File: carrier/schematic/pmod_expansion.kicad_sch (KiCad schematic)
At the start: 14 parts, among them J19001 DS1024-2x6R2, SW19001 DSHP04TSGER, U19001 SY6280AAC, U19002 TPD4E1U06, U19003 TPD4E1U06

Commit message: bom: sourcing risk+cost report + C1591->C14663 (Extended->Basic 100n)
Stream F — live JLCPCB/LCSC sourcing pass over all 95 distinct BOM parts.

Report: carrier/manufacturing/SOURCING.md — per-part stock / Basic-vs-Extended
/ unit price / risk + flagged second sources, and a rollup (94 parts post-swap,
64 Extended of which 2 Preferred -> 62 feeder fees = ~$186, 15 parts <5k stock,
6 procurement-critical <300). Data from the JLCPCB parts API (live).

Applied swap (only clean Basic drop-in on the board): 100 nF 0603 decoupling
C1591 (Samsung CL10B104KB8NNNC, Extended, 2.08M) -> C14663 (YAGEO
CC0603KRX7R9BB104, Basic, 17.8M). IDENTICAL 100nF/50V/X7R/+-10%/0603, same
footprint+symbol -> netlist & render byte-identical; ratings.py already carries
C14663 with matching ratings. Merges 71 Extended + 12 existing-Basic positions
onto one 83-piece Basic line: removes one Extended feeder fee, cheaper unit,
8.5x more stock.

Everything else is REPORT-ONLY: every other Extended part is
Extended-by-necessity (no JLC-Basic equivalent — precise E96 values, specialty
ICs/connectors) or has only a footprint-mismatched / MPN-ambiguous alternate.
Also flagged (not fixed): C25750 ("40.2k" power:R1) currently resolves on LCSC
to a 120k 0402 part — a data-integrity bug; recommend C12447 after intent check.

Gates: part-rules PASS (132 checks, 0 findings); board PASS (33 sheets, golden
renders 33/33 match, DRC 0); selftest 59/59; m1_rc PASS; pytest 219 passed.
BOM regen deterministic (md5 stable).

Co-Authored-By: Claude Opus 4.8 <noreply@anthropic.com>
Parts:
- C19001, C19002, C19003: LCSC C1591 -> C14663
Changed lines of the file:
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@@
 		(property
 			"LCSC"
-			"C1591"
+			"C14663"
 			(at 29.21 66.04 0)
 			(effects
@@
 		(property
 			"LCSC"
-			"C1591"
+			"C14663"
 			(at 39.37 66.04 0)
 			(effects
@@
 		(property
 			"LCSC"
-			"C1591"
+			"C14663"
 			(at 49.53 66.04 0)
 			(effects

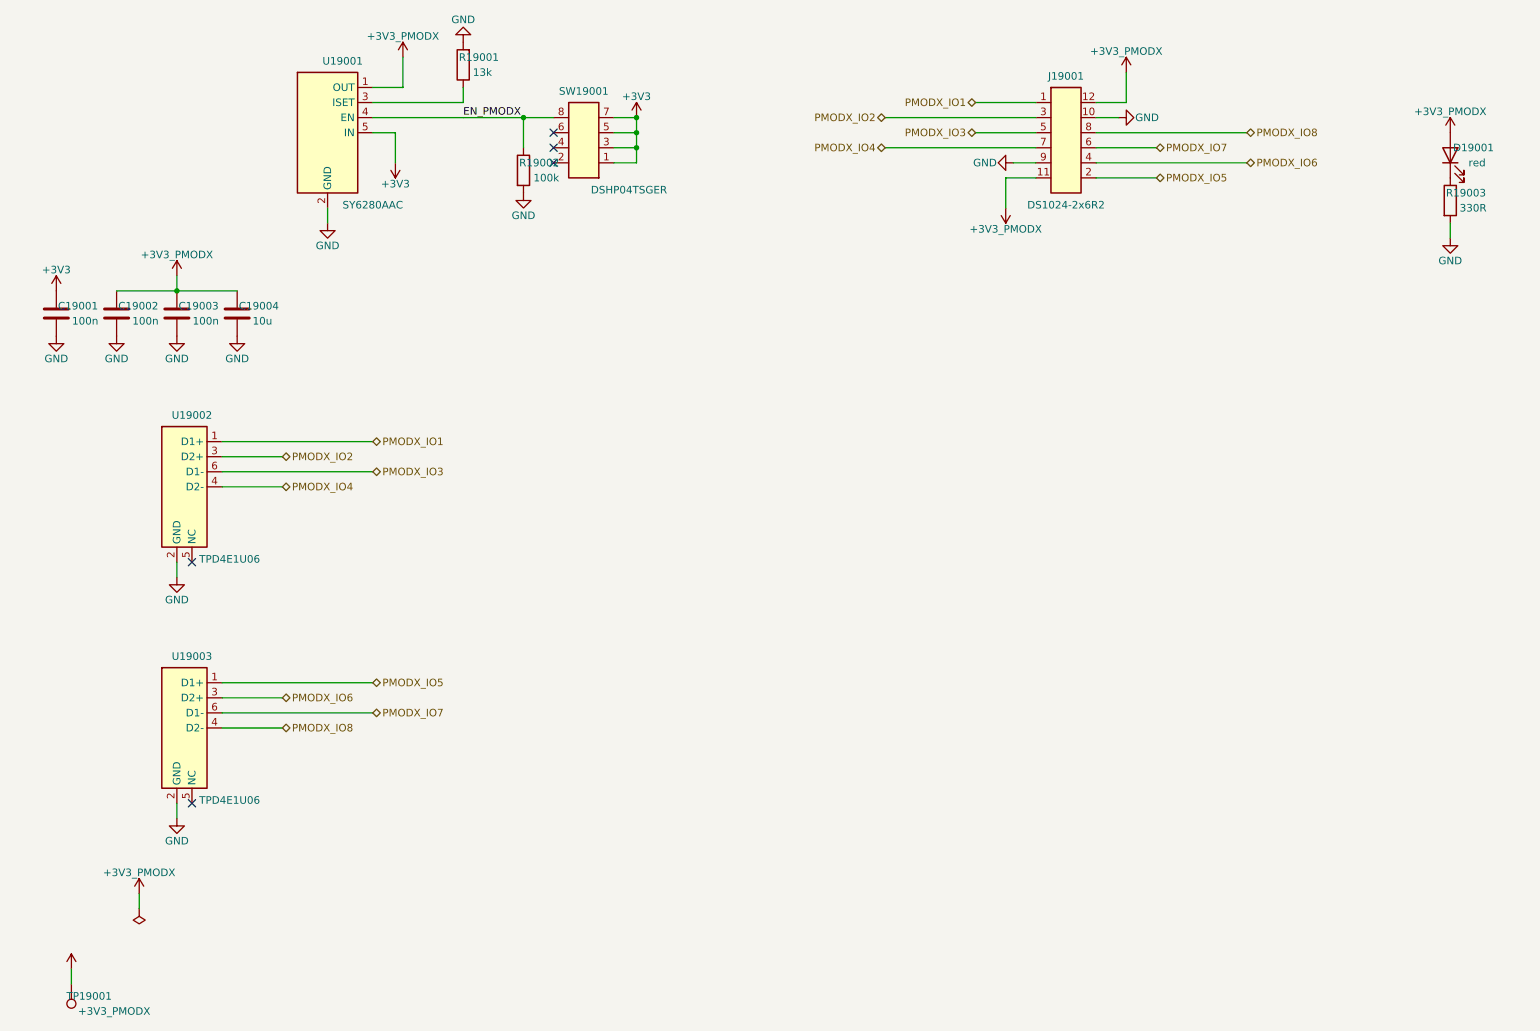
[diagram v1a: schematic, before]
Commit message: carrier: 4 confirmed datasheet-audit fixes (crystal CL, LED Vf, SY6280 Cin, LVC125 doc)
All four adversarially re-verified against the datasheet + schematic before
applying:

- usb_jtag-1 (crystal load caps): Y1 (KDS DSX321G, CL=12pF) had two 22pF load
  caps presenting ~15pF -> 8MHz pulled ~-50..-90ppm (outside ±20ppm). 22p->16p
  C0G 0603 (Cext = 2·(CL-~4pF stray)); LCSC C162205 (Murata GRM1885C1H160JA01D,
  16pF C0G 50V 0603, live-verified).
- usb_jtag-2 (SN74LVC125A): removed the false "Ioff partial-power-down" docstring
  claim (TI SCAS290T has no such spec); powered-rail Hi-Z holds via the normal
  3-state OE pull-up. Series back-feed Rs documented as a DNP/layout reservation
  (forcing them overflows the A3 sheet; not fitted).
- io_misc-1 (user LED current): +3V3_USER_LED through 1k gave ~0.2mA (invisible)
  for the high-Vf (~3.1V) green/blue/white LEDs. Per-colour Rs: red keeps 1k
  (~1.3mA); green/blue/white -> 200R (C8218), ~1-3.5mA, within the 5mA rating.
- expansion-1 (SY6280 Cin): the load-switch IN pin had only 100n; added the
  datasheet-mandated 10uF (C15850) bulk at U1.IN, kept the 100n.

BOM VALUES now 0 unverified (white LED C2290 catalogued). Regression: board 33
+ golden match, all gates PASS, selftest 59, m1_rc, pytest 242 — green.

Co-Authored-By: Claude Opus 4.8 <noreply@anthropic.com>
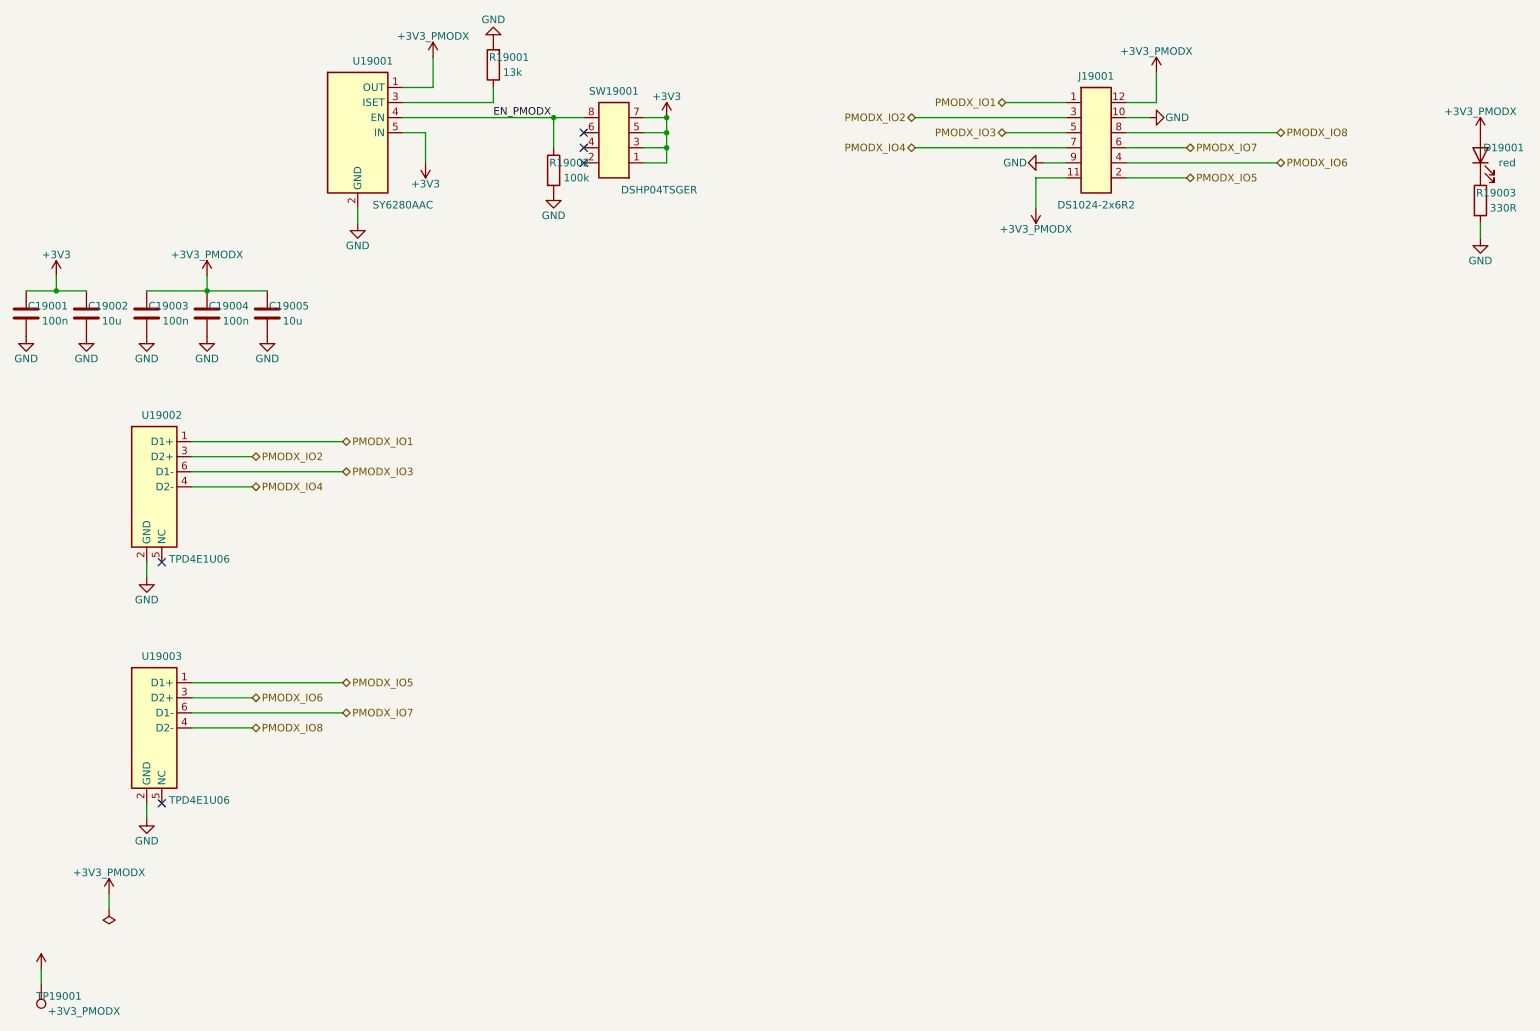
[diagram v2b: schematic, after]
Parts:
- added TP19001: +3V3_PMODX, TestPoint:TestPoint_Pad_D1.5mm, symbol Connector:TestPoint
- C19002: value 100n -> 10u; footprint Capacitor_SMD:C_0603_1608Metric -> Capacitor_SMD:C_0805_2012Metric; LCSC C14663 -> C15850
- C19004: value 10u -> 100n; footprint Capacitor_SMD:C_0805_2012Metric -> Capacitor_SMD:C_0603_1608Metric; LCSC C15850 -> C14663
- C19005: renamed from U19002; value TPD4E1U06 -> 10u; footprint TPD4E1U06DBVR:TPD4E1U06DBVR -> Capacitor_SMD:C_0805_2012Metric; symbol TPD4E1U06DBVR:TPD4E1U06DBVR -> Device:C; LCSC C124691 -> C15850
- D19001: renamed from R19003; value 330R -> red; footprint Resistor_SMD:R_0603_1608Metric -> LED_SMD:LED_0603_1608Metric; symbol Device:R -> Device:LED; LCSC C23138 -> C2286
- R19003: renamed from TP19001; value +3V3_PMODX -> 330R; footprint TestPoint:TestPoint_Pad_D1.5mm -> Resistor_SMD:R_0603_1608Metric; symbol Connector:TestPoint -> Device:R; BOM exclude -> (none); LCSC (none) -> C23138
- U19003: renamed from D19001; value red -> TPD4E1U06; footprint LED_SMD:LED_0603_1608Metric -> TPD4E1U06DBVR:TPD4E1U06DBVR; symbol Device:LED -> TPD4E1U06DBVR:TPD4E1U06DBVR; LCSC C2286 -> C124691
- renumbered U19003 to U19002
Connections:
- net +3V3: now also C19002.1
- net +3V3_PMODX: now also C19005.1, D19001.2 (A), TP19001.1; no longer C19002.1, R19003.1, U19003.2 (A)
- net GND: now also R19003.2, U19003.2 (GND); no longer D19001.2
- net PMODX_IO1: now also U19002.1 (D1+); no longer C19005.1 (D1+)
- net PMODX_IO2: now also U19002.3 (D2+); no longer C19005.3 (D2+)
- net PMODX_IO3: now also U19002.6 (D1-); no longer C19005.6 (D1-)
- net PMODX_IO4: now also U19002.4 (D2-); no longer C19005.4 (D2-)
- net PMODX_IO5: now also U19003.1 (D1+); no longer U19002.1 (D1+)
- net PMODX_IO6: now also U19003.3 (D2+); no longer U19002.3 (D2+)
- net PMODX_IO7: now also U19003.6 (D1-); no longer U19002.6 (D1-)
- net PMODX_IO8: now also U19003.4 (D2-); no longer U19002.4 (D2-)
- net at D19001.1 (K): now also R19003.1; no longer U19003.1 (K)
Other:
- moved on the sheet: C19001, C19002, C19003, C19004, J19001, R19001, R19002, SW19001, U19001, U19002

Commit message: fix(silk): tighten 6 sheet titles overflowing the title-block cell (M6)
The audit flagged 6 sheet titles whose text overflowed the KiCad title-block
Title cell, crossing the border/zone rules (LAW 1). Root cause: the authored
Circuit titles were longer than the cell renders (the fit boundary is ~58 chars
of typical text; these were 55-73). Tightened all 6 at the source (display-only
strings, no info-loss of the essentials, cannot affect netlist/routing — board
.kicad_pcb byte-unchanged):
- board_services 73->47, pmod_expansion 65->45, mechanical 60->50,
  usb_jtag 59->38, usb_jtag_connector 58->42, power_som 55->37.
Render-confirmed: board_services + mechanical (the longest) now end well inside
the cell. The gallery description table (carrier/README.md) regenerated to match.
666 tests pass at HEAD; the 3 title-asserting tests (som_j1/j2/j3) are untouched.

Co-Authored-By: Claude Opus 4.8 <noreply@anthropic.com>
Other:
- title: Pmod expansion port (2x6, bank 13, low-cap ESD, manual-gated 3V3) -> Pmod expansion (2x6, bank 13, ESD, gated 3V3)
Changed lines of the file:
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@@
 	(paper "A4")
 	(title_block
-		(title "Pmod expansion port (2x6, bank 13, low-cap ESD, manual-gated 3V3)")
+		(title "Pmod expansion (2x6, bank 13, ESD, gated 3V3)")
 		(company "Zynq SoM Carrier")
 		(comment 1 "pmod_expansion — generated by schgen (do not hand-edit)")
